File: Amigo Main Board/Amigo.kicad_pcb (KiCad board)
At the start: 2 copper layers, 50 x 50 mm, 43 parts, among them J1 USB_C_Receptacle_USB2.0_16P, J2 Conn_01x02, J3 SH1106 OLED, J4 MAX98357A, J5 DRV8833, J6 ButtonRibbonConnector, SW1 SW_Push, SW2 SW_Push, U1 TP4056-42-ESOP8, U2 AP2112K-3.3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

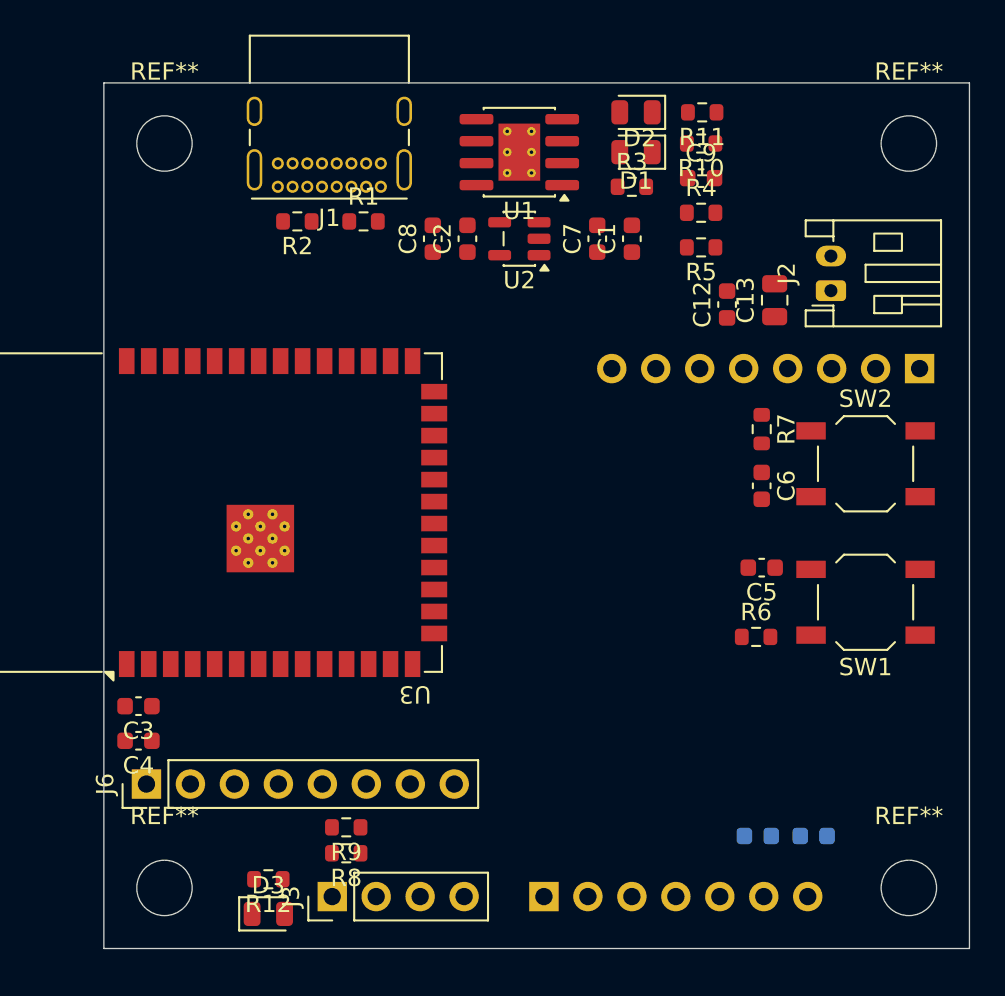
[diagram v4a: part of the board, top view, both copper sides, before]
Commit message: Fixed all DRC errors, Added groundpour
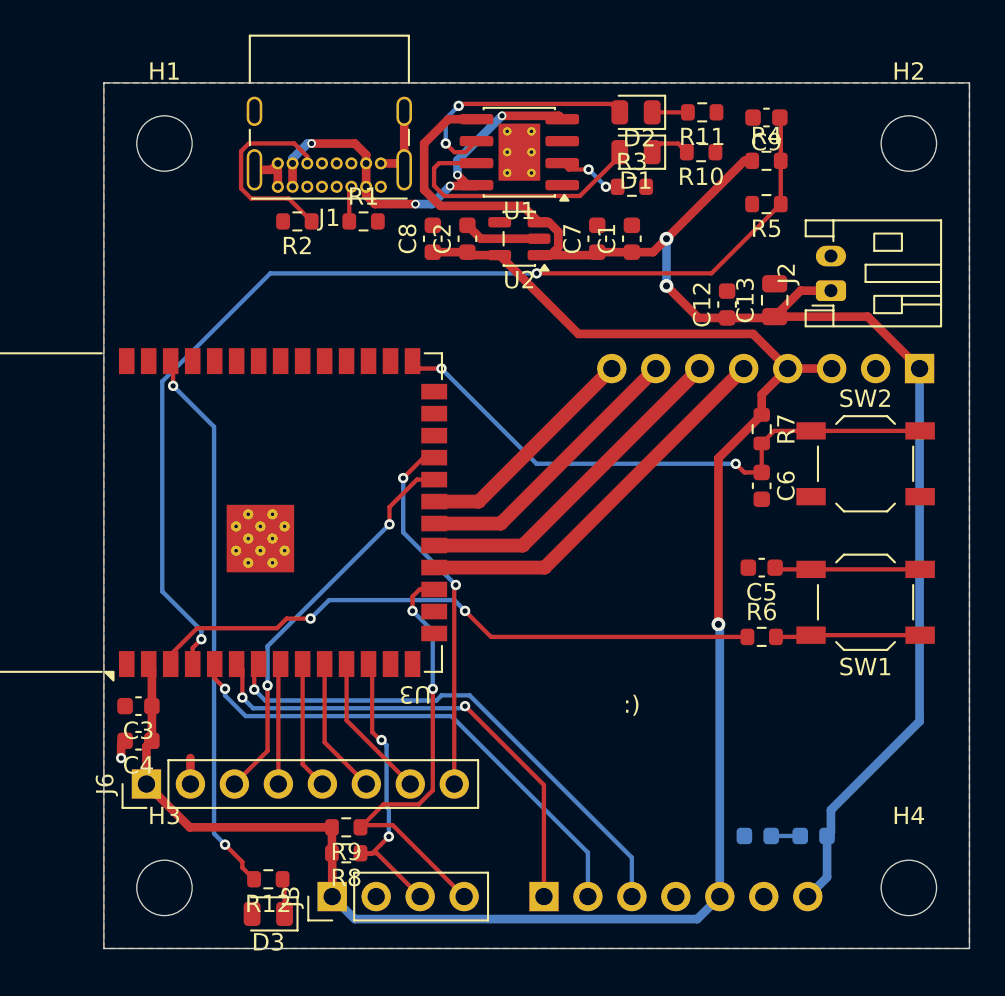
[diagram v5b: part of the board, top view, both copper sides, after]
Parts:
- moved C9 5.15 mm to (50.3, 14.0), turned to 180 degrees
- moved R4 4.82 mm to (50.3, 16.5)
- moved R5 4.53 mm to (50.3, 19.0)
- moved R10 0.50 mm to (46.5, 16.0)
- moved R6 0.33 mm to (50.0, 44.0)
- turned D3 to 180 degrees
- renumbered REF** to H1, REF** to H2, REF** to H3, REF** to H4
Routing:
- net +3V3: track 0.00 -> 104.4 mm, vias 0 -> 1
- net BAT+: track 0.00 -> 88.2 mm, vias 0 -> 2
- net BAT_SENSE: track 0.00 -> 62.5 mm, vias 0 -> 2
- net EN: track 0.00 -> 36.0 mm, vias 0 -> 2
- net IO0: track 0.00 -> 34.0 mm, vias 0 -> 2
- net LED_STATUS: track 0.00 -> 31.9 mm, vias 0 -> 2
- net AUDIO_DOUT: track 0.00 -> 29.9 mm, vias 0 -> 1
- net AUDIO_BCLK: track 0.00 -> 29.3 mm, vias 0 -> 1
- net AUDIO_LRC_WS: track 0.00 -> 28.1 mm, vias 0 -> 2
- net OLED_SCL: track 0.00 -> 25.9 mm, vias 0 -> 2
- net VBUS_5V: track 0.00 -> 25.3 mm, vias 0 -> 5
- net BUTTON_ROW_0: track 0.00 -> 22.9 mm, vias 0 -> 2
- net MOTOR_A_IN1: track 0.00 -> 22.6 mm
- net BUTTON_COL_2: track 0.00 -> 21.3 mm, vias 0 -> 2
- net MOTOR_A_IN2: track 0.00 -> 19.6 mm
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- added copper zone on B.Cu, net GND
- added copper zone on F.Cu, net GND
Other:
- board text added: ":)"

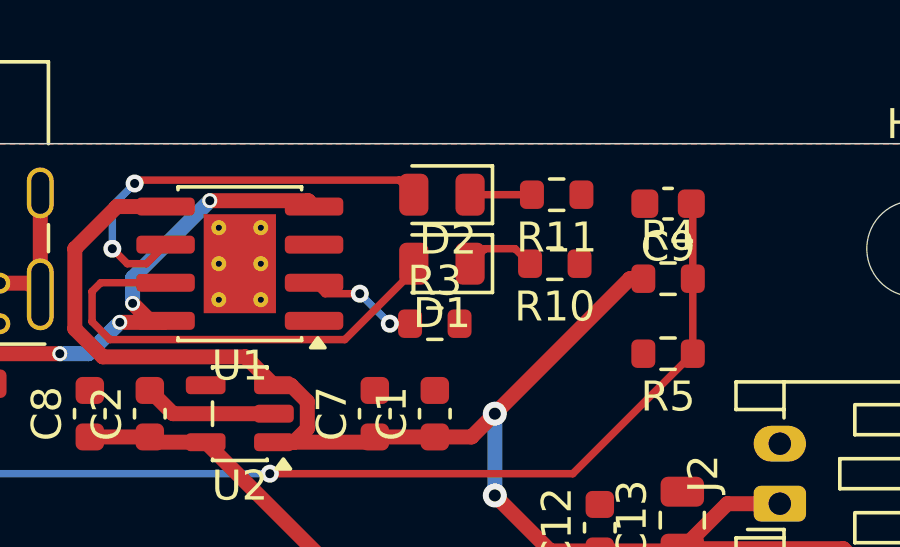
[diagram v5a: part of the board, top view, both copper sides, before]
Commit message: fixed LED polarity
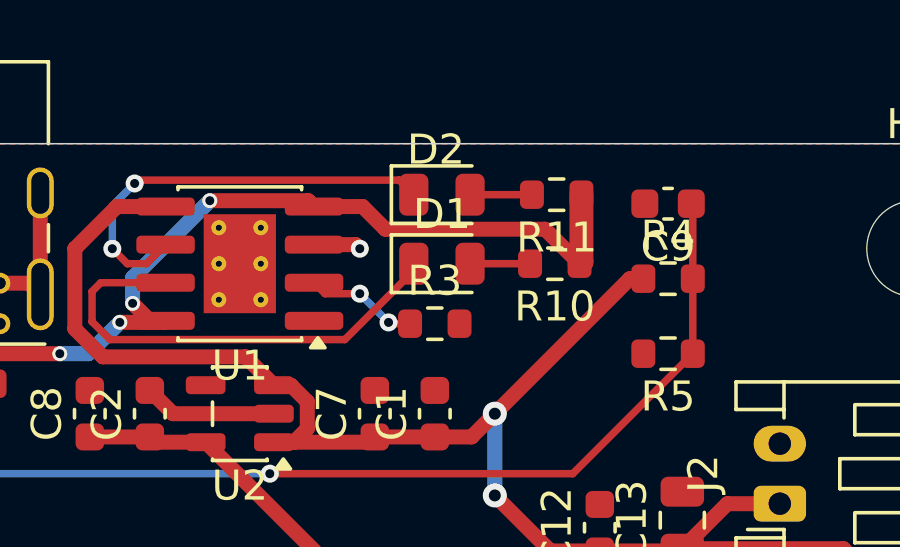
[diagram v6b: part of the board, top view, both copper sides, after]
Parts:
- turned D1 to 0 degrees
- turned D2 to 0 degrees
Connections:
- R10 pad 1: GND -> VBUS_5V
- R10 pad 2: Net-(D1-K) -> Net-(D1-A)
- R11 pad 1: GND -> VBUS_5V
- R11 pad 2: Net-(D2-K) -> Net-(D2-A)
- U1 pad 6: Net-(D2-A) -> Net-(D2-K)
- U1 pad 7: Net-(D1-A) -> Net-(D1-K)
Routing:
- net Net-(D1-A): track 15.7 -> 2.00 mm
- net Net-(D1-K): track 2.41 -> 15.7 mm
- net Net-(D2-K): track 2.06 -> 14.3 mm, vias 0 -> 2
- net Net-(D2-A): track 14.3 -> 2.06 mm, vias 2 -> 0
- net VBUS_5V: track 25.3 -> 37.2 mm
- net GND: track 14.9 -> 16.5 mm, vias 1 -> 2

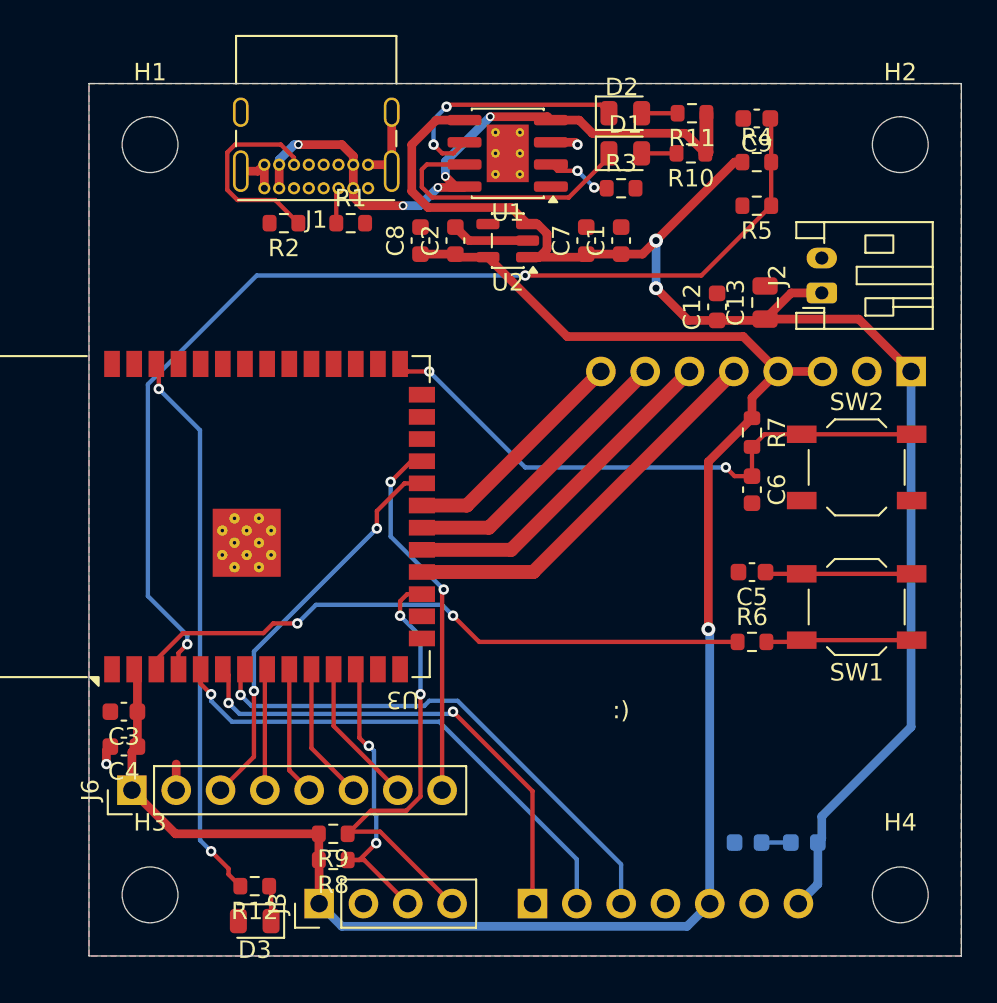
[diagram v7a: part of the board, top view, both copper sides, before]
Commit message: Finished wiring up the new OLED
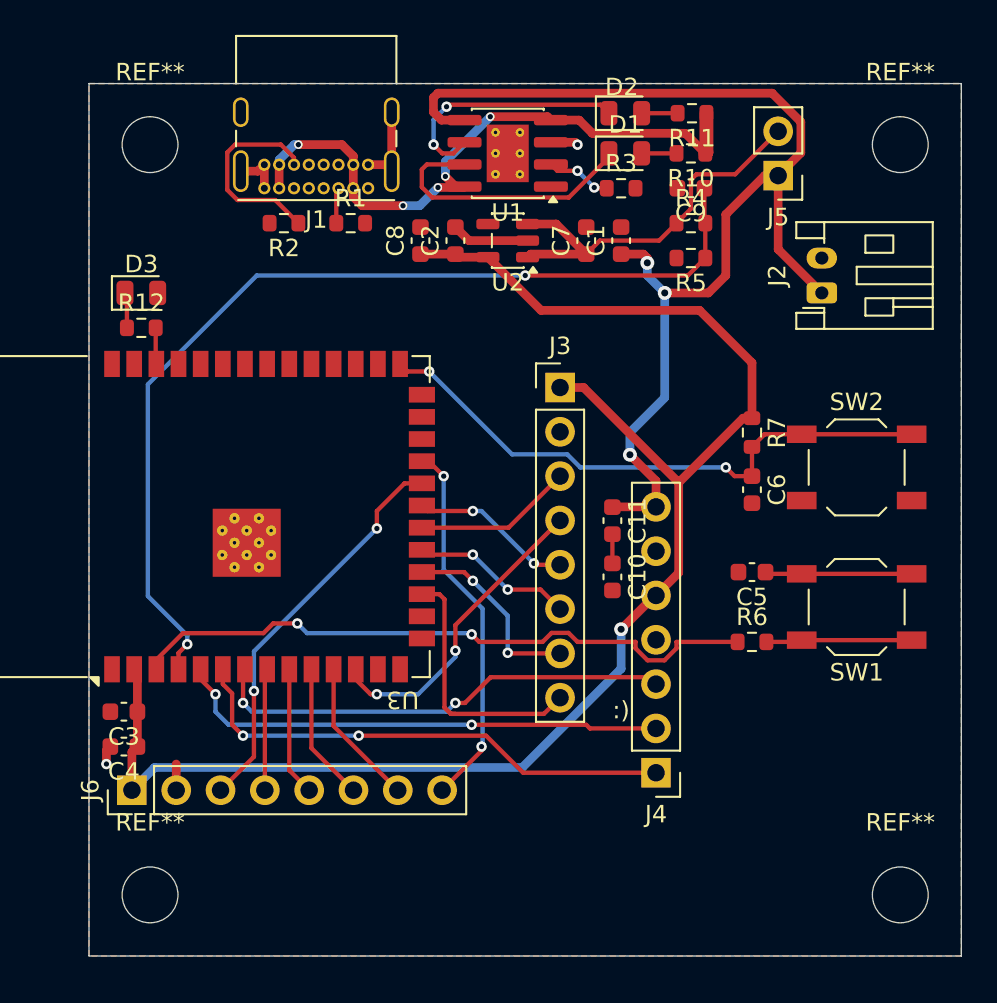
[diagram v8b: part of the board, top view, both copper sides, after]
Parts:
- removed C12: 100nF, Capacitor_SMD:C_0603_1608Metric
- removed C13: 10µF, Capacitor_SMD:C_0805_2012Metric
- removed H1, H2, H3, H4: MountingHole_3.2mm_M3, MountingHole:MountingHole_3.2mm_M3
- removed R8, R9: 4.7k, Resistor_SMD:R_0603_1608Metric
- added REF**: MountingHole_3.2mm_M3, MountingHole:MountingHole_3.2mm_M3, F.Cu at (15.5, 58.5)
- added REF**: MountingHole_3.2mm_M3, MountingHole:MountingHole_3.2mm_M3, F.Cu at (58.5, 58.5)
- added REF**: MountingHole_3.2mm_M3, MountingHole:MountingHole_3.2mm_M3, F.Cu at (58.5, 15.5)
- added REF**: MountingHole_3.2mm_M3, MountingHole:MountingHole_3.2mm_M3, F.Cu at (15.5, 15.5)
- C10, C11, J4: moved to F.Cu
- J3: value SH1106 OLED -> OLED; footprint Connector_PinHeader_2.54mm:PinHeader_1x04_P2.54mm_Vertical -> Connector_PinHeader_2.54mm:PinHeader_1x08_P2.54mm_Vertical
- J5: value DRV8833 -> Rocker Switch; footprint Connector_PinHeader_2.54mm:PinHeader_1x08_P2.54mm_Vertical -> Connector_PinHeader_2.54mm:PinHeader_1x02_P2.54mm_Vertical; moved to F.Cu
- moved D3 36.6 mm to (15.0, 24.0), turned to 0 degrees
- moved R12 32.7 mm to (15.0, 26.0), turned to 0 degrees
- moved J3 32.6 mm to (39.0, 29.4), turned to 0 degrees
- moved C11 21.5 mm to (42.0, 37.0), turned to -90 degrees
- moved C10 17.1 mm to (42.0, 40.3), turned to -90 degrees
- moved J5 13.6 mm to (51.5, 17.3), turned to 180 degrees
- moved J4 10.3 mm to (44.5, 51.5), turned to 180 degrees
- moved C9 5.50 mm to (46.5, 18.0)
- moved R4 5.15 mm to (46.5, 20.0)
- moved R5 4.82 mm to (46.5, 22.0)
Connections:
- C7 pad 1: BAT+ -> BAT_SW
- J3 pad 3: OLED_SDA -> LCD_CS
- J3 pad 4: OLED_SCL -> LCD_RST
- J5 pad 2: GND -> BAT_SW
- R4 pad 1: BAT+ -> BAT_SW
- U2 pad 1: BAT+ -> BAT_SW
- U2 pad 3: BAT+ -> BAT_SW
- U3 pad 12: OLED_SDA -> LCD_RST
- U3 pad 17: OLED_SCL -> LCD_BL
- U3 pad 18: MOTOR_A_IN1 -> LCD_SCK
- U3 pad 19: MOTOR_A_IN2 -> LCD_MOSI
- U3 pad 20: MOTOR_B_IN1 -> LCD_CS
- U3 pad 21: MOTOR_B_IN2 -> LCD_DC
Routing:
- net LED_STATUS: track 31.9 -> 2.08 mm, vias 2 -> 0
- net OLED_SCL: track 25.9 -> 0.00 mm, vias 2 -> 0
- net BAT_SW: track 0.00 -> 22.6 mm
- net MOTOR_A_IN1: track 22.6 -> 0.00 mm
- net BAT+: track 88.2 -> 67.6 mm, vias 2 -> 3
- net MOTOR_A_IN2: track 19.6 -> 0.00 mm
- net LCD_RST: track 0.00 -> 17.8 mm, vias 0 -> 2
- net OLED_SDA: track 17.0 -> 0.00 mm, vias 2 -> 0
- net MOTOR_B_IN1: track 16.5 -> 0.00 mm
- net LCD_BL: track 0.00 -> 15.0 mm
- net +3V3: track 104.4 -> 89.7 mm
- net MOTOR_B_IN2: track 13.4 -> 0.00 mm
- net LCD_SCK: track 0.00 -> 11.1 mm, vias 0 -> 2
- net LCD_DC: track 0.00 -> 9.33 mm, vias 0 -> 2
- net LCD_MOSI: track 0.00 -> 9.33 mm, vias 0 -> 2
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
